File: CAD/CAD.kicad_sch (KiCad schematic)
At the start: 9 parts, among them M1 Motor_Servo_Hitec, U1 HTRC11001T

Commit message: added pcb layout v0.1
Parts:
- removed U1: HTRC11001T, Package_SO:SOIC-14_3.9x8.7mm_P1.27mm, symbol RF_RFID:HTRC11001T
- added U1: RFID_RC522, symbol I2C:RFID_RC522
- R2: renamed from R?; footprint (none) -> Resistor_SMD:R_2512_6332Metric_Pad1.40x3.35mm_HandSolder
- gave numbers to parts that had none: 5
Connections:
- net +5V: now also A1.5 (+5V), M1.2 (+), U2. (VCC), U1. (SDA)
- net GND: now also U1. (SDA)
- net at A1.13 (SDA/A4), U2. (VCC): now also U1. (SDA)
- net at A1.14 (SCL/A5), U2. (VCC): now also U1. (SDA)
- removed net VCC: A1.5 (+5V), M1.2 (+), U2. (VCC)
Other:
- company: (none) -> ECE411 Group 10 Practicum
- title: ECE411 Group 10 Practicum -> Laser Security System - Schematic

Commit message: updated pcb layout with template
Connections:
- new net: A1.13 (SDA/A4), U1. (SDA), U2. (VCC)
- new net: A1.14 (SCL/A5), U1. (SDA), U2. (VCC)
- no-connect marks 0 -> 21
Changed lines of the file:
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@@
   (junction (at 91.44 86.36) (diameter 0) (color 0 0 0 0)
   )
+  (no_connect (at 129.54 96.52))
+  (no_connect (at 129.54 93.98))
+  (no_connect (at 129.54 88.9))
+  (no_connect (at 154.94 101.6))
+  (no_connect (at 154.94 99.06))
+  (no_connect (at 139.7 109.22))
+  (no_connect (at 144.78 109.22))
+  (no_connect (at 154.94 86.36))
+  (no_connect (at 154.94 83.82))
+  (no_connect (at 154.94 81.28))
+  (no_connect (at 154.94 76.2))
+  (no_connect (at 154.94 71.12))
+  (no_connect (at 154.94 66.04))
+  (no_connect (at 129.54 83.82))
+  (no_connect (at 129.54 81.28))
+  (no_connect (at 129.54 78.74))
+  (no_connect (at 129.54 76.2))
+  (no_connect (at 129.54 73.66))
+  (no_connect (at 129.54 71.12))
+  (no_connect (at 129.54 68.58))
+  (no_connect (at 129.54 66.04))
   (wire (pts (xy 147.32 52.07) (xy 147.32 55.88))
     (stroke (width 0) (type default) (color 0 0 0 0))

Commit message: added BOM
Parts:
- added R3, R4: 4.7k, Resistor_SMD:R_1206_3216Metric_Pad1.30x1.75mm_HandSolder, symbol Device:R_US
- LD1, PR1, SW1: footprint (none) -> Connector_PinHeader_2.00mm:PinHeader_1x02_P2.00mm_Vertical
- M1: footprint (none) -> Connector_PinHeader_2.00mm:PinHeader_1x03_P2.00mm_Vertical
- R1: footprint (none) -> Resistor_SMD:R_1206_3216Metric_Pad1.30x1.75mm_HandSolder
- R2: footprint Resistor_SMD:R_2512_6332Metric_Pad1.40x3.35mm_HandSolder -> Resistor_SMD:R_1206_3216Metric_Pad1.30x1.75mm_HandSolder
- U1: footprint (none) -> Connector_PinHeader_2.00mm:PinHeader_1x04_P2.00mm_Vertical
- U2: footprint (none) -> Connector_PinHeader_1.00mm:PinHeader_1x04_P1.00mm_Vertical
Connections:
- net +5V: now also U1.3 (3.3V), U2.3 (VCC), R3.2, R4.1; no longer A1.8 (VIN), U1. (SDA), U2. (VCC)
- net GND: now also A1.29 (GND), A1.7 (GND), U1.4 (GND), U2.4 (GND); no longer U1. (SDA), U2. (VCC)
- new net: A1.14 (SCL/A5), R4.2, U1.1 (SCL), U2.1 (SCL)
- new net: A1.13 (SDA/A4), R3.1, U1.2 (SDA), U2.2 (SDA)
- no-connect marks 21 -> 19

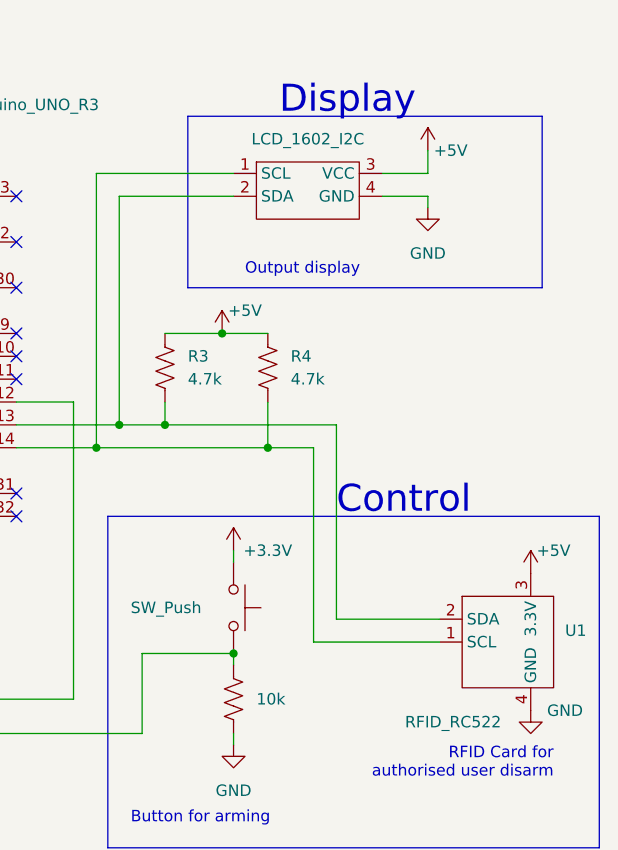
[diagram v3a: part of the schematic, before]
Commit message: Fixed pcb footprints, passing DRC!
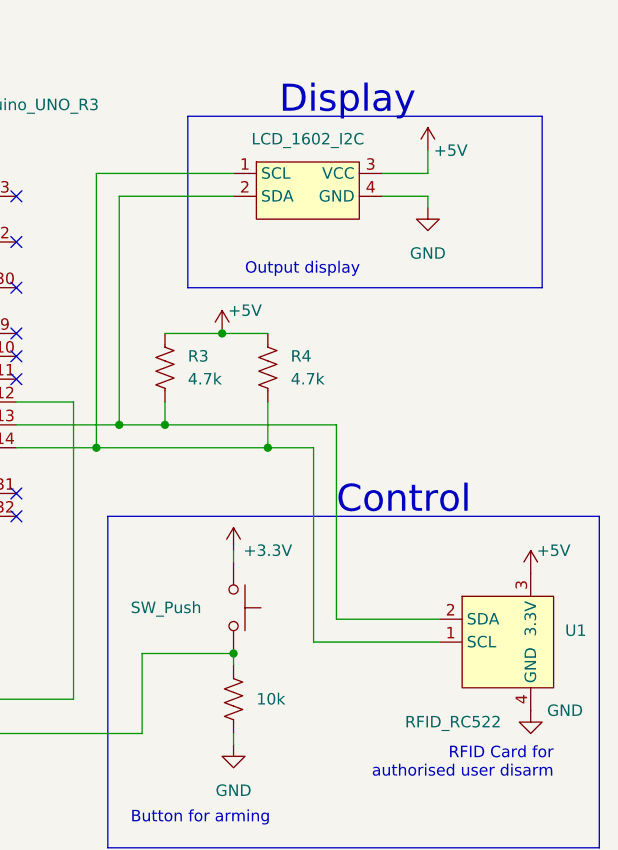
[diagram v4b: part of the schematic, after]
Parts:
- U2: footprint Connector_PinHeader_1.00mm:PinHeader_1x04_P1.00mm_Vertical -> Connector_PinHeader_2.00mm:PinHeader_1x04_P2.00mm_Vertical
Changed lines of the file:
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@@
   (title_block
     (title "Laser Security System - Schematic")
-    (date "10/26/2022")
-    (rev "0.5")
+    (date "2022-11-10")
+    (rev "1")
     (company "ECE411 Group 10 Practicum")
   )
@@
     )
     (property "Value" "LCD_1602_I2C" (id 1) (at 187.325 59.69 0))
-    (property "Footprint" "Connector_PinHeader_1.00mm:PinHeader_1x04_P1.00mm_Vertical" (id 2) (at 184.15 67.31 0)
+    (property "Footprint" "Connector_PinHeader_2.00mm:PinHeader_1x04_P2.00mm_Vertical" (id 2) (at 184.15 67.31 0)
       (effects (font (size 1.27 1.27)) hide)
     )
@@
       (effects (font (size 1.27 1.27)) hide)
     )
+    (pin "1")
+    (pin "2")
+    (pin "3")
     (pin "4")
-    (pin "1")
-    (pin "2")
-    (pin "3")
   )
   (symbol (lib_id "power:+5V") (at 200.66 60.96 0) (unit 1)
@@
       (effects (font (size 1.27 1.27)) hide)
     )
+    (pin "1")
+    (pin "2")
     (pin "3")
     (pin "4")
-    (pin "1")
-    (pin "2")
   )
   (symbol (lib_id "power:+3.3V") (at 144.78 49.53 0) (unit 1)
@@
     )
     (path "/21a2029b-6123-4a1b-8ece-2df0a086f340"
-      (reference "U2") (unit 1) (value "LCD_1602_I2C") (footprint "Connector_PinHeader_1.00mm:PinHeader_1x04_P1.00mm_Vertical")
-    )
-  )
+      (reference "U2") (unit 1) (value "LCD_1602_I2C") (footprint "Connector_PinHeader_2.00mm:PinHeader_1x04_P2.00mm_Vertical")
+    )
+  )

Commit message: Final CAD
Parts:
- added PR1, PR2, PR4: R_Photo, Connector_PinHeader_2.54mm:PinHeader_2x04_P2.54mm_Vertical, symbol Device:R_Photo
- added Q1: 2N7002, Package_TO_SOT_SMD:SOT-223-3_TabPin2, symbol Transistor_FET:2N7002
- added R1, R5, R6, R8: 10k, Resistor_SMD:R_1206_3216Metric_Pad1.30x1.75mm_HandSolder, symbol Device:R_US
- added SW2: SW_Push, Connector_PinHeader_2.54mm:PinHeader_1x02_P2.54mm_Vertical, symbol Switch:SW_Push
- LD1: footprint Connector_PinHeader_2.00mm:PinHeader_1x02_P2.00mm_Vertical -> Connector_PinSocket_2.54mm:PinSocket_2x04_P2.54mm_Vertical
- M1: footprint Connector_PinHeader_2.00mm:PinHeader_1x03_P2.00mm_Vertical -> Connector_PinHeader_2.54mm:PinHeader_2x03_P2.54mm_Vertical
- PR3: renamed from PR1; footprint Connector_PinHeader_2.00mm:PinHeader_1x02_P2.00mm_Vertical -> Connector_PinHeader_2.54mm:PinHeader_2x04_P2.54mm_Vertical
- R7: renamed from R1; value 100 -> 10k
- SW1: footprint Connector_PinHeader_2.00mm:PinHeader_1x02_P2.00mm_Vertical -> Connector_PinHeader_2.54mm:PinHeader_1x02_P2.54mm_Vertical
- U1: footprint Connector_PinHeader_2.00mm:PinHeader_1x04_P2.00mm_Vertical -> Connector_PinSocket_2.54mm:PinSocket_2x04_P2.54mm_Vertical
- U2: footprint Connector_PinHeader_2.00mm:PinHeader_1x04_P2.00mm_Vertical -> Connector_PinSocket_2.54mm:PinSocket_1x04_P2.54mm_Vertical
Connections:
- net +3.3V: now also U1.1 (3.3V), SW2.2; no longer LD1.1 (K), PR3.1
- net +5V: now also LD1.2 (A), PR3.1, U2.1 (VCC), PR1.1, PR2.1, PR4.1; no longer M1.2 (+), U1.3 (3.3V), U2.3 (VCC)
- net GND: now also U1. (GND), Q1.2 (S), R1.2, R5.2, R6.2, R8.2; no longer A1.23 (D8), LD1.2 (A), U1.4 (GND)
- net at R3.1, U2.2 (SCL): now also A1.32 (SCL/A5); no longer A1.13 (SDA/A4), U1.2 (SDA)
- net at R2.1, SW1.1: now also A1.22 (D7); no longer A1.28 (D13)
- net at PR3.2, R7.1: now also A1.10 (A1); no longer A1.12 (A3)
- net at A1.25 (D10): now also U1.6 (SDA); no longer M1.1 (PWM)
- net at A1.11 (A2): now also PR2.2, R6.1
- net at A1.17 (D2): now also M1.5
- net at A1.18 (D3): now also M1.6
- net at A1.19 (D4): now also M1.4
- net at A1.20 (D5): now also M1.2 (PWM)
- net at A1.21 (D6): now also R1.1, SW2.1
- net at A1.24 (D9): now also U1.2 (RST)
- net at A1.26 (D11): now also U1.8 (MOSI)
- net at A1.27 (D12): now also U1.5 (MISO)
- net at A1.31 (SDA/A4): now also R4.2, U2.3 (SDA)
- net at A1.9 (A0): now also PR4.2, R8.1
- new net: A1.12 (A3), PR1.2, R5.1
- new net: A1.23 (D8), Q1.1 (G)
- new net: LD1.1 (K), Q1.3 (D)
- new net: A1.28 (D13), U1.7 (SLK)
- new net +9V: M1.1 (+)
- now unconnected: A1.14 (SCL/A5)
- no-connect marks 19 -> 8
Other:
- note added: "9V from offboard buck converter"
- note added: "Additional pins reserved for different motor types"
- note added: "Pullup Resistors for I2C"
- note added: "Vin driven by 120VAC -> 5V 2A wall plug"
- moved on the sheet: PR3, R3, R4
